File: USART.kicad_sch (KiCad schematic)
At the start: 5 parts, among them J11 Conn_01x02_Female

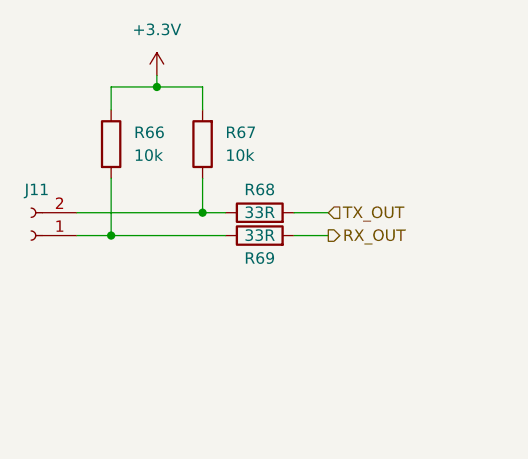
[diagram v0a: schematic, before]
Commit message: pcb is in progress, finishing H-bridge layout
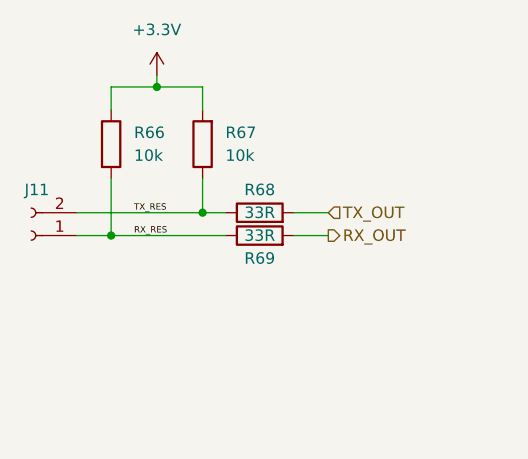
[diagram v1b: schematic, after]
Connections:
- net TX_RES: now reaches J11.2 (Pin_2), R67.1, R68.1
- net RX_RES: now reaches J11.1 (Pin_1), R66.2, R69.1
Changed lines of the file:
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@@
     (stroke (width 0) (type default) (color 0 0 0 0))
+  )
+  (label "RX_RES" (at 138.43 97.79 0)
+    (effects (font (size 0.7 0.7)) (justify left bottom))
+  )
+  (label "TX_RES" (at 138.43 95.25 0)
+    (effects (font (size 0.7 0.7)) (justify left bottom))
   )
   (hierarchical_label "RX_OUT" (shape output) (at 160.02 97.79 0)

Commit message: changed power loss detection schematic, changed tvs diodes on other type, added two more caps on 3v3 line, change indicator leds resistors
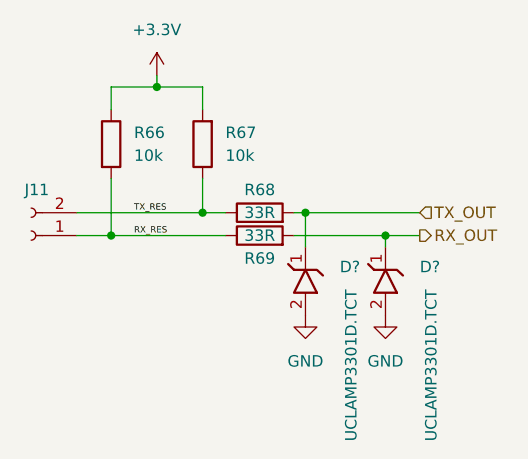
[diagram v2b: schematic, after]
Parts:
- added D? (x2): UCLAMP3301D.TCT, _Diodes:UCLAMP3301D.TCT, symbol _Diodes:UCLAMP3301D.TCT
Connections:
- net RX_OUT: now also D?.1
- net TX_OUT: now also D?.1
- new net GND: D?.2, D?.2
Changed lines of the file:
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@@
 (kicad_sch (version 20211123) (generator eeschema)
   (paper "A4")
+  (junction (at 157.48 95.25) (diameter 0) (color 0 0 0 0)
+  )
   (junction (at 140.97 81.28) (diameter 0) (color 0 0 0 0)
   )
   (junction (at 135.89 97.79) (diameter 0) (color 0 0 0 0)
   )
+  (junction (at 166.37 97.79) (diameter 0) (color 0 0 0 0)
+  )
   (junction (at 146.05 95.25) (diameter 0) (color 0 0 0 0)
   )
@@
     (stroke (width 0) (type default) (color 0 0 0 0))
   )
-  (wire (pts (xy 156.21 97.79) (xy 160.02 97.79))
+  (wire (pts (xy 156.21 97.79) (xy 166.37 97.79))
     (stroke (width 0) (type default) (color 0 0 0 0))
   )
@@
     (stroke (width 0) (type default) (color 0 0 0 0))
   )
-  (wire (pts (xy 156.21 95.25) (xy 160.02 95.25))
+  (wire (pts (xy 156.21 95.25) (xy 157.48 95.25))
     (stroke (width 0) (type default) (color 0 0 0 0))
   )
@@
     (stroke (width 0) (type default) (color 0 0 0 0))
   )
+  (wire (pts (xy 157.48 95.25) (xy 170.18 95.25))
+    (stroke (width 0) (type default) (color 0 0 0 0))
+  )
+  (wire (pts (xy 166.37 97.79) (xy 170.18 97.79))
+    (stroke (width 0) (type default) (color 0 0 0 0))
+  )
+  (wire (pts (xy 157.48 95.25) (xy 157.48 99.06))
+    (stroke (width 0) (type default) (color 0 0 0 0))
+  )
   (wire (pts (xy 146.05 95.25) (xy 148.59 95.25))
+    (stroke (width 0) (type default) (color 0 0 0 0))
+  )
+  (wire (pts (xy 166.37 97.79) (xy 166.37 99.06))
     (stroke (width 0) (type default) (color 0 0 0 0))
   )
@@
     (effects (font (size 0.7 0.7)) (justify left bottom))
   )
-  (hierarchical_label "RX_OUT" (shape output) (at 160.02 97.79 0)
+  (hierarchical_label "RX_OUT" (shape output) (at 170.18 97.79 0)
     (effects (font (size 1.27 1.27)) (justify left))
   )
-  (hierarchical_label "TX_OUT" (shape input) (at 160.02 95.25 0)
+  (hierarchical_label "TX_OUT" (shape input) (at 170.18 95.25 0)
     (effects (font (size 1.27 1.27)) (justify left))
+  )
+  (symbol (lib_id "power:GND") (at 166.37 106.68 0) (unit 1)
+    (in_bom yes) (on_board yes) (fields_autoplaced)
+    (property "Reference" "#PWR?" (id 0) (at 166.37 113.03 0)
+      (effects (font (size 1.27 1.27)) hide)
+    )
+    (property "Value" "GND" (id 1) (at 166.37 111.76 0))
+    (property "Footprint" "" (id 2) (at 166.37 106.68 0)
+      (effects (font (size 1.27 1.27)) hide)
+    )
+    (property "Datasheet" "" (id 3) (at 166.37 106.68 0)
+      (effects (font (size 1.27 1.27)) hide)
+    )
+    (pin "1")
+  )
+  (symbol (lib_id "_Diodes:UCLAMP3301D.TCT") (at 157.48 110.49 0) (unit 1)
+    (in_bom yes) (on_board yes)
+    (property "Reference" "D?" (id 0) (at 161.29 101.2755 0)
+      (effects (font (size 1.27 1.27)) (justify left))
+    )
+    (property "Value" "UCLAMP3301D.TCT" (id 1) (at 162.56 120.65 90)
+      (effects (font (size 1.27 1.27)) (justify left))
+    )
+    (property "Footprint" "_Diodes:UCLAMP3301D.TCT" (id 2) (at 157.48 110.49 0)
+      (effects (font (size 1.27 1.27)) hide)
+    )
+    (property "Datasheet" "" (id 3) (at 157.48 110.49 0)
+      (effects (font (size 1.27 1.27)) hide)
+    )
+    (pin "1")
+    (pin "2")
   )
   (symbol (lib_id "Device:R") (at 146.05 87.63 180) (unit 1)
@@
     (pin "2")
   )
+  (symbol (lib_id "_Diodes:UCLAMP3301D.TCT") (at 166.37 110.49 0) (unit 1)
+    (in_bom yes) (on_board yes)
+    (property "Reference" "D?" (id 0) (at 170.18 101.2755 0)
+      (effects (font (size 1.27 1.27)) (justify left))
+    )
+    (property "Value" "UCLAMP3301D.TCT" (id 1) (at 171.45 120.65 90)
+      (effects (font (size 1.27 1.27)) (justify left))
+    )
+    (property "Footprint" "_Diodes:UCLAMP3301D.TCT" (id 2) (at 166.37 110.49 0)
+      (effects (font (size 1.27 1.27)) hide)
+    )
+    (property "Datasheet" "" (id 3) (at 166.37 110.49 0)
+      (effects (font (size 1.27 1.27)) hide)
+    )
+    (pin "1")
+    (pin "2")
+  )
+  (symbol (lib_id "power:GND") (at 157.48 106.68 0) (unit 1)
+    (in_bom yes) (on_board yes) (fields_autoplaced)
+    (property "Reference" "#PWR?" (id 0) (at 157.48 113.03 0)
+      (effects (font (size 1.27 1.27)) hide)
+    )
+    (property "Value" "GND" (id 1) (at 157.48 111.76 0))
+    (property "Footprint" "" (id 2) (at 157.48 106.68 0)
+      (effects (font (size 1.27 1.27)) hide)
+    )
+    (property "Datasheet" "" (id 3) (at 157.48 106.68 0)
+      (effects (font (size 1.27 1.27)) hide)
+    )
+    (pin "1")
+  )
   (symbol (lib_id "power:+3.3V") (at 140.97 80.01 0) (unit 1)

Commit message: updated footprints on board and sgematics
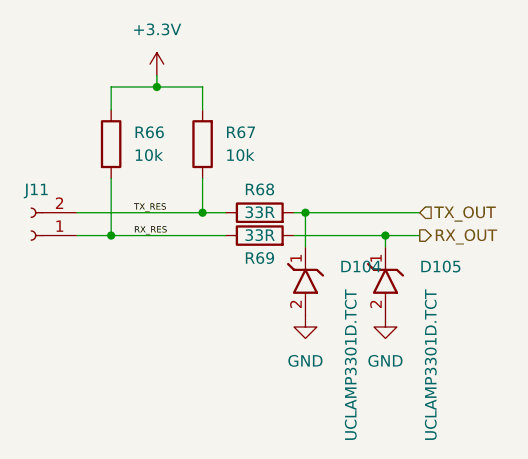
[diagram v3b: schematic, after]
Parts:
- gave numbers to parts that had none: 2
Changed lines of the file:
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@@
   (symbol (lib_id "power:GND") (at 166.37 106.68 0) (unit 1)
     (in_bom yes) (on_board yes) (fields_autoplaced)
-    (property "Reference" "#PWR?" (id 0) (at 166.37 113.03 0)
+    (property "Reference" "#PWR0218" (id 0) (at 166.37 113.03 0)
       (effects (font (size 1.27 1.27)) hide)
     )
@@
   (symbol (lib_id "_Diodes:UCLAMP3301D.TCT") (at 157.48 110.49 0) (unit 1)
     (in_bom yes) (on_board yes)
-    (property "Reference" "D?" (id 0) (at 161.29 101.2755 0)
+    (property "Reference" "D104" (id 0) (at 161.29 101.2755 0)
       (effects (font (size 1.27 1.27)) (justify left))
     )
@@
   (symbol (lib_id "_Diodes:UCLAMP3301D.TCT") (at 166.37 110.49 0) (unit 1)
     (in_bom yes) (on_board yes)
-    (property "Reference" "D?" (id 0) (at 170.18 101.2755 0)
+    (property "Reference" "D105" (id 0) (at 170.18 101.2755 0)
       (effects (font (size 1.27 1.27)) (justify left))
     )
@@
   (symbol (lib_id "power:GND") (at 157.48 106.68 0) (unit 1)
     (in_bom yes) (on_board yes) (fields_autoplaced)
-    (property "Reference" "#PWR?" (id 0) (at 157.48 113.03 0)
+    (property "Reference" "#PWR0219" (id 0) (at 157.48 113.03 0)
       (effects (font (size 1.27 1.27)) hide)
     )
